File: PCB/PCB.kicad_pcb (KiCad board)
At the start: 2 copper layers, 120 x 60 mm, 62 parts, among them J1 USB_C_Receptacle_USB2.0_16P, J2 Conn_01x15, J3 Conn_01x15, Q2 IRLML2060, SW1 TSA016A2526B, SW2 TSA016A2526B, SW3 TSA016A2526B, U1 RP2040, U2 USBLC6-2SC6, U3 NCP1117ST33T3G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

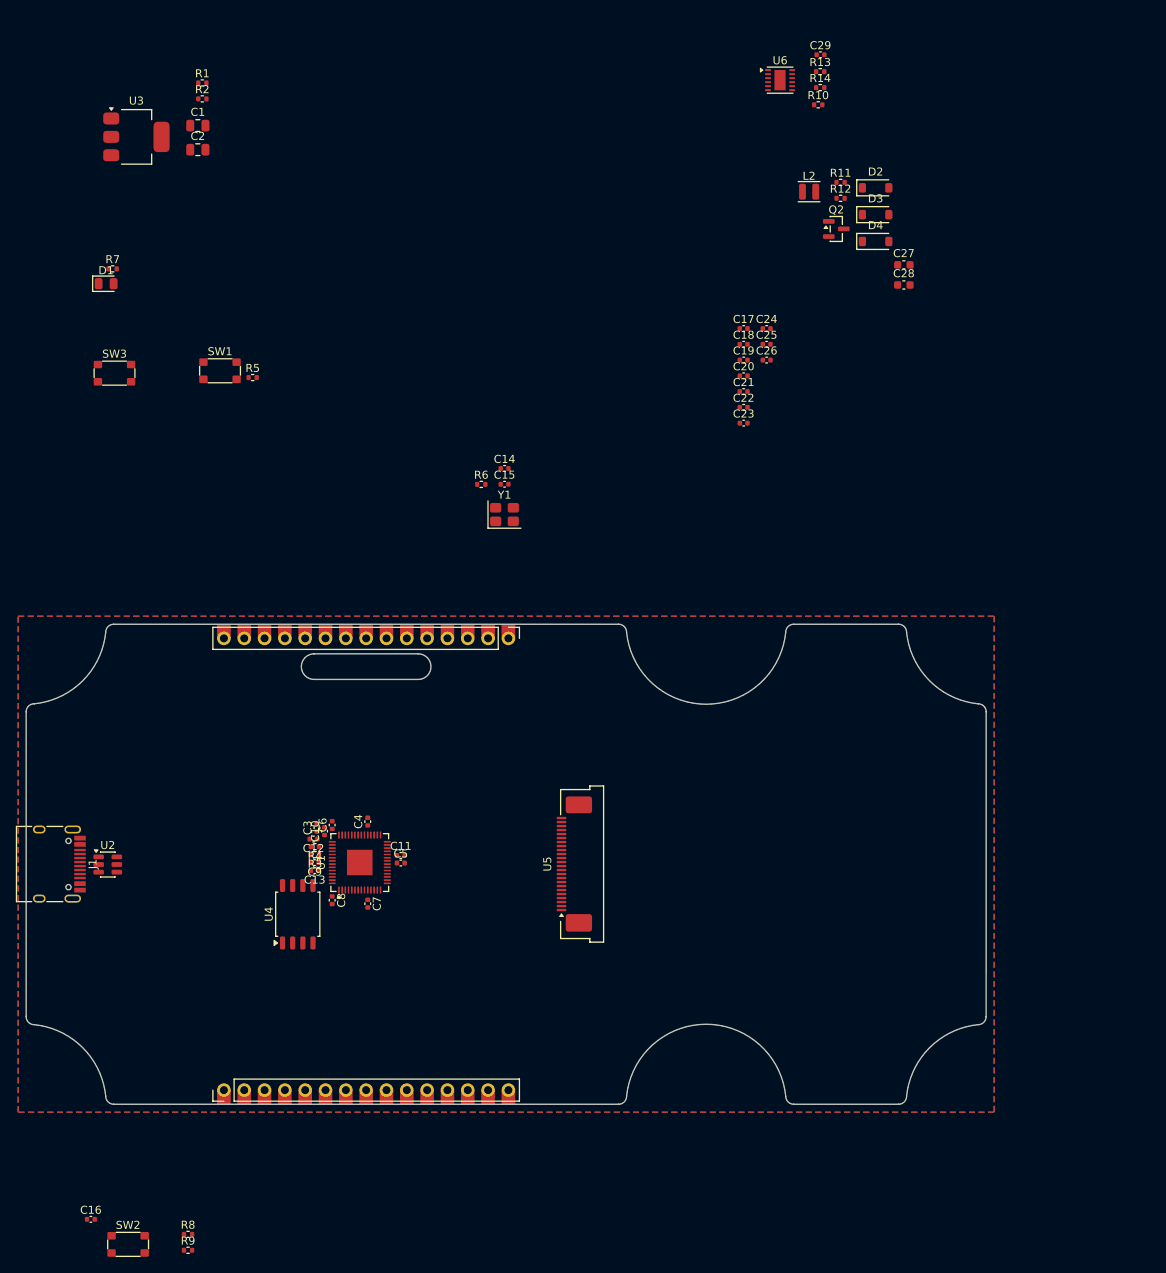
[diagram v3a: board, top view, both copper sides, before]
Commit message: aligning crystal and LDO
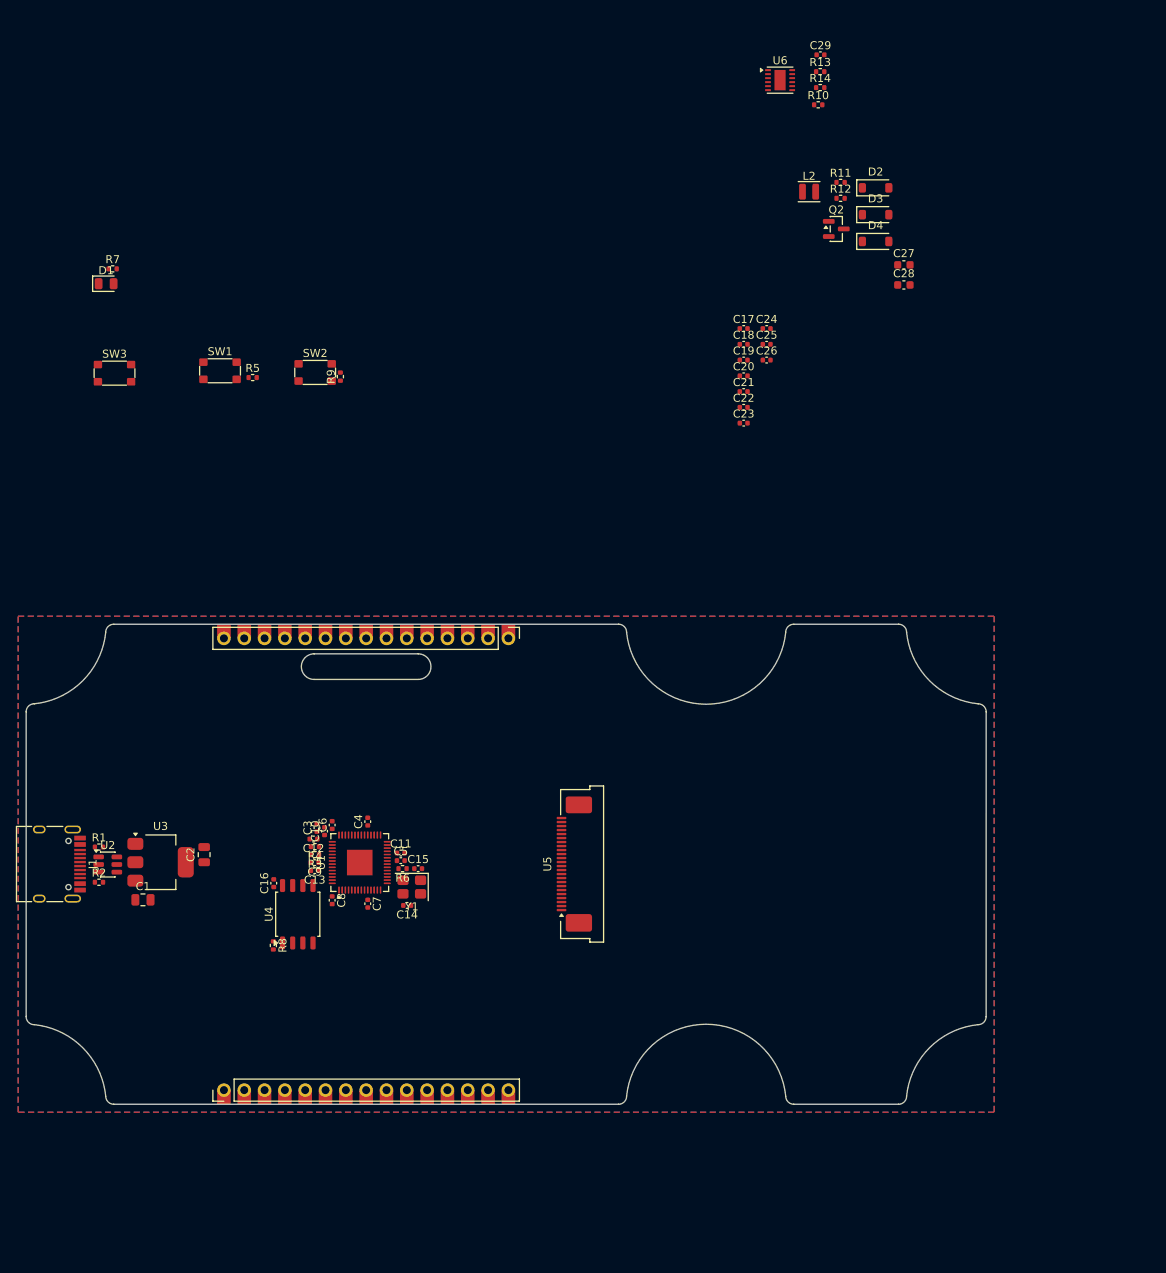
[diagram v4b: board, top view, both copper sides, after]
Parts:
- moved SW2 111.5 mm to (106.1, 63.5)
- moved R9 110.9 mm to (109.3, 64.0), turned to 90 degrees
- moved R2 98.8 mm to (79.1, 127.2)
- moved C1 97.0 mm to (84.6, 129.4)
- moved R1 96.4 mm to (79.1, 122.8)
- moved U3 90.7 mm to (86.8, 124.8)
- moved C2 88.1 mm to (92.2, 123.8), turned to 90 degrees
- moved C14 56.0 mm to (117.6, 130.2), turned to 180 degrees
- moved C15 49.2 mm to (119.0, 125.5)
- moved R6 49.0 mm to (117.0, 125.5), turned to 180 degrees
- moved Y1 48.0 mm to (118.2, 127.8), turned to 180 degrees
- moved C16 47.8 mm to (101.0, 127.4), turned to 90 degrees
- moved R8 37.7 mm to (100.9, 135.2), turned to -90 degrees
- moved C11 0.30 mm to (116.8, 123.6)
- moved C5 0.30 mm to (116.8, 124.5)

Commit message: aligning eink stuff
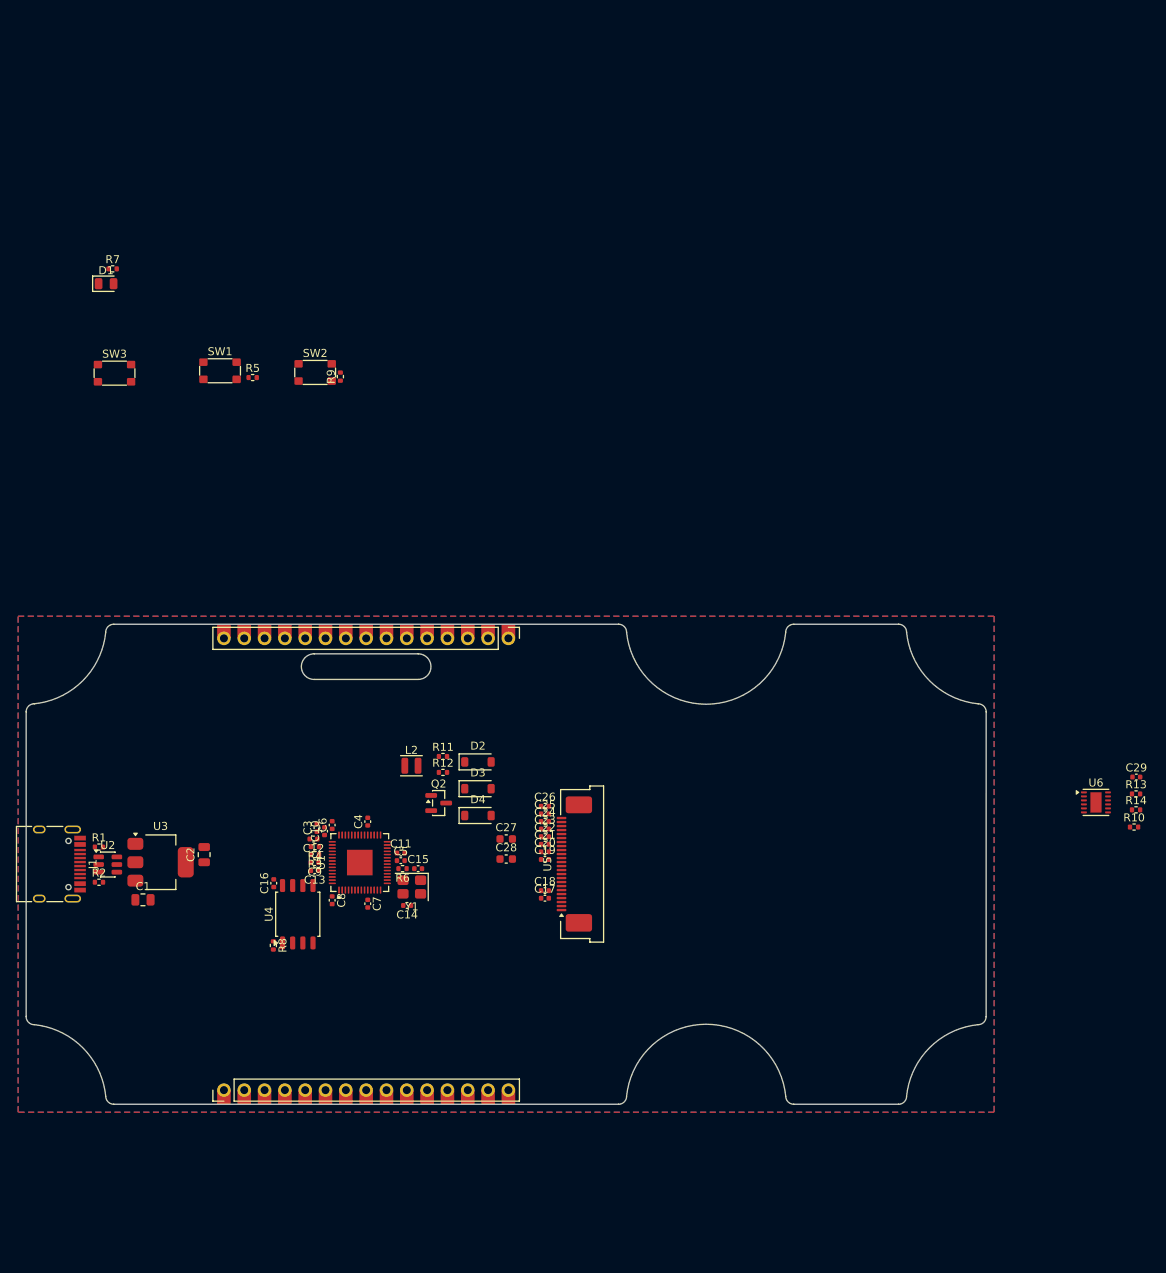
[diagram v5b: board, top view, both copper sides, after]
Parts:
- moved C29 98.5 mm to (208.8, 114.1)
- moved R10 98.5 mm to (208.5, 120.3)
- moved R13 98.5 mm to (208.7, 116.2)
- moved R14 98.5 mm to (208.7, 118.2)
- moved U6 98.5 mm to (203.7, 117.3)
- moved C27 87.3 mm to (130.0, 121.8)
- moved C28 87.3 mm to (130.0, 124.3)
- moved D2 87.3 mm to (126.5, 112.2)
- moved D3 87.3 mm to (126.5, 115.6)
- moved D4 87.3 mm to (126.5, 118.9)
- moved L2 87.3 mm to (118.2, 112.7)
- moved Q2 87.3 mm to (121.6, 117.3)
- moved R11 87.3 mm to (122.1, 111.5)
- moved R12 87.3 mm to (122.1, 113.5)
- moved C17 75.4 mm to (134.8, 129.2)
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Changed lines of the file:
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@@
 	(footprint "Capacitor_SMD:C_0402_1005Metric"
 		(layer "F.Cu")
-		(at 162.56 61.98)
+		(at 134.85 117.75)
 		(descr "Capacitor SMD 0402 (1005 Metric), square (rectangular) end terminal, IPC-7351 nominal, (Body size source: IPC-SM-782 page 76, https://www.pcb-3d.com/wordpress/wp-content/uploads/ipc-sm-782a_amendment_1_and_2.pdf), generated with kicad-footprint-generator")
 		(tags "capacitor")
@@
 	(footprint "Diode_SMD:D_SOD-123"
 		(layer "F.Cu")
-		(at 176.18 40.45)
+		(at 126.475 112.21)
 		(descr "SOD-123")
 		(tags "SOD-123")
@@
 	(footprint "Capacitor_SMD:C_0402_1005Metric"
 		(layer "F.Cu")
-		(at 169.2875 23.82)
+		(at 208.77 114.1)
 		(descr "Capacitor SMD 0402 (1005 Metric), square (rectangular) end terminal, IPC-7351 nominal, (Body size source: IPC-SM-782 page 76, https://www.pcb-3d.com/wordpress/wp-content/uploads/ipc-sm-782a_amendment_1_and_2.pdf), generated with kicad-footprint-generator")
 		(tags "capacitor")
@@
 	(footprint "Inductor_SMD:L_Sunlord_SWPA252010S"
 		(layer "F.Cu")
-		(at 167.865 40.93)
+		(at 118.16 112.69)
 		(descr "Inductor, Sunlord, SWPA252010S, 2.5x2.0x1.0mm, (https://www.sunlordinc.com/UploadFiles/PDF_Cat/20120704094224784.pdf), generated with kicad-footprint-generator gen_inductor.py")
 		(tags "swpa")
@@
 	(footprint "Resistor_SMD:R_0402_1005Metric"
 		(layer "F.Cu")
-		(at 169.255 27.92)
+		(at 208.7375 118.2)
 		(descr "Resistor SMD 0402 (1005 Metric), square (rectangular) end terminal, IPC-7351 nominal, (Body size source: IPC-SM-782 page 72, https://www.pcb-3d.com/wordpress/wp-content/uploads/ipc-sm-782a_amendment_1_and_2.pdf), generated with kicad-footprint-generator")
 		(tags "resistor")
@@
 	(footprint "Capacitor_SMD:C_0402_1005Metric"
 		(layer "F.Cu")
-		(at 162.56 58.04)
+		(at 134.85 119.65)
 		(descr "Capacitor SMD 0402 (1005 Metric), square (rectangular) end terminal, IPC-7351 nominal, (Body size source: IPC-SM-782 page 76, https://www.pcb-3d.com/wordpress/wp-content/uploads/ipc-sm-782a_amendment_1_and_2.pdf), generated with kicad-footprint-generator")
 		(tags "capacitor")
@@
 	(footprint "Diode_SMD:D_SOD-123"
 		(layer "F.Cu")
-		(at 176.18 47.15)
+		(at 126.475 118.91)
 		(descr "SOD-123")
 		(tags "SOD-123")
@@
 	(footprint "Capacitor_SMD:C_0402_1005Metric"
 		(layer "F.Cu")
-		(at 159.69 60.01)
+		(at 134.85 128.3)
 		(descr "Capacitor SMD 0402 (1005 Metric), square (rectangular) end terminal, IPC-7351 nominal, (Body size source: IPC-SM-782 page 76, https://www.pcb-3d.com/wordpress/wp-content/uploads/ipc-sm-782a_amendment_1_and_2.pdf), generated with kicad-footprint-generator")
 		(tags "capacitor")
@@
 	(footprint "Capacitor_SMD:C_0402_1005Metric"
 		(layer "F.Cu")
-		(at 159.69 58.04)
+		(at 134.85 129.25)
 		(descr "Capacitor SMD 0402 (1005 Metric), square (rectangular) end terminal, IPC-7351 nominal, (Body size source: IPC-SM-782 page 76, https://www.pcb-3d.com/wordpress/wp-content/uploads/ipc-sm-782a_amendment_1_and_2.pdf), generated with kicad-footprint-generator")
 		(tags "capacitor")
@@
 	(footprint "Package_TO_SOT_SMD:SOT-23"
 		(layer "F.Cu")
-		(at 171.2675 45.59)
+		(at 121.5625 117.35)
 		(descr "SOT, 3 Pin (JEDEC TO-236 Var AB https://www.jedec.org/document_search?search_api_views_fulltext=TO-236), generated with kicad-footprint-generator ipc_gullwing_generator.py")
 		(tags "SOT TO_SOT_SMD")
@@
 	(footprint "Capacitor_SMD:C_0402_1005Metric"
 		(layer "F.Cu")
-		(at 159.69 61.98)
+		(at 134.85 124.4)
 		(descr "Capacitor SMD 0402 (1005 Metric), square (rectangular) end terminal, IPC-7351 nominal, (Body size source: IPC-SM-782 page 76, https://www.pcb-3d.com/wordpress/wp-content/uploads/ipc-sm-782a_amendment_1_and_2.pdf), generated with kicad-footprint-generator")
 		(tags "capacitor")
@@
 	(footprint "Capacitor_SMD:C_0603_1608Metric"
 		(layer "F.Cu")
-		(at 179.715 50.08)
+		(at 130.01 121.84)
 		(descr "Capacitor SMD 0603 (1608 Metric), square (rectangular) end terminal, IPC-7351 nominal, (Body size source: IPC-SM-782 page 76, https://www.pcb-3d.com/wordpress/wp-content/uploads/ipc-sm-782a_amendment_1_and_2.pdf), generated with kicad-footprint-generator")
 		(tags "capacitor")
@@
 	(footprint "Capacitor_SMD:C_0402_1005Metric"
 		(layer "F.Cu")
-		(at 159.69 67.89)
+		(at 134.85 121.55)
 		(descr "Capacitor SMD 0402 (1005 Metric), square (rectangular) end terminal, IPC-7351 nominal, (Body size source: IPC-SM-782 page 76, https://www.pcb-3d.com/wordpress/wp-content/uploads/ipc-sm-782a_amendment_1_and_2.pdf), generated with kicad-footprint-generator")
 		(tags "capacitor")
@@
 	(footprint "Diode_SMD:D_SOD-123"
 		(layer "F.Cu")
-		(at 176.18 43.8)
+		(at 126.475 115.56)
 		(descr "SOD-123")
 		(tags "SOD-123")
@@
 	(footprint "Capacitor_SMD:C_0603_1608Metric"
 		(layer "F.Cu")
-		(at 179.715 52.59)
+		(at 130.01 124.35)
 		(descr "Capacitor SMD 0603 (1608 Metric), square (rectangular) end terminal, IPC-7351 nominal, (Body size source: IPC-SM-782 page 76, https://www.pcb-3d.com/wordpress/wp-content/uploads/ipc-sm-782a_amendment_1_and_2.pdf), generated with kicad-footprint-generator")
 		(tags "capacitor")
@@
 	(footprint "Capacitor_SMD:C_0402_1005Metric"
 		(layer "F.Cu")
-		(at 162.56 60.01)
+		(at 134.85 118.7)
 		(descr "Capacitor SMD 0402 (1005 Metric), square (rectangular) end terminal, IPC-7351 nominal, (Body size source: IPC-SM-782 page 76, https://www.pcb-3d.com/wordpress/wp-content/uploads/ipc-sm-782a_amendment_1_and_2.pdf), generated with kicad-footprint-generator")
 		(tags "capacitor")
@@
 	(footprint "Capacitor_SMD:C_0402_1005Metric"
 		(layer "F.Cu")
-		(at 159.69 69.86)
+		(at 134.85 120.6)
 		(descr "Capacitor SMD 0402 (1005 Metric), square (rectangular) end terminal, IPC-7351 nominal, (Body size source: IPC-SM-782 page 76, https://www.pcb-3d.com/wordpress/wp-content/uploads/ipc-sm-782a_amendment_1_and_2.pdf), generated with kicad-footprint-generator")
 		(tags "capacitor")
@@
 	(footprint "Resistor_SMD:R_0402_1005Metric"
 		(layer "F.Cu")
-		(at 169.255 25.93)
+		(at 208.7375 116.21)
 		(descr "Resistor SMD 0402 (1005 Metric), square (rectangular) end terminal, IPC-7351 nominal, (Body size source: IPC-SM-782 page 72, https://www.pcb-3d.com/wordpress/wp-content/uploads/ipc-sm-782a_amendment_1_and_2.pdf), generated with kicad-footprint-generator")
 		(tags "resistor")
@@
 	(footprint "Resistor_SMD:R_0402_1005Metric"
 		(layer "F.Cu")
-		(at 169.0075 30.07)
+		(at 208.49 120.35)
 		(descr "Resistor SMD 0402 (1005 Metric), square (rectangular) end terminal, IPC-7351 nominal, (Body size source: IPC-SM-782 page 72, https://www.pcb-3d.com/wordpress/wp-content/uploads/ipc-sm-782a_amendment_1_and_2.pdf), generated with kicad-footprint-generator")
 		(tags "resistor")
@@
 	(footprint "Capacitor_SMD:C_0402_1005Metric"
 		(layer "F.Cu")
-		(at 159.69 63.95)
+		(at 134.85 123.45)
 		(descr "Capacitor SMD 0402 (1005 Metric), square (rectangular) end terminal, IPC-7351 nominal, (Body size source: IPC-SM-782 page 76, https://www.pcb-3d.com/wordpress/wp-content/uploads/ipc-sm-782a_amendment_1_and_2.pdf), generated with kicad-footprint-generator")
 		(tags "capacitor")
@@
 	(footprint "Capacitor_SMD:C_0402_1005Metric"
 		(layer "F.Cu")
-		(at 159.69 65.92)
+		(at 134.85 122.5)
 		(descr "Capacitor SMD 0402 (1005 Metric), square (rectangular) end terminal, IPC-7351 nominal, (Body size source: IPC-SM-782 page 76, https://www.pcb-3d.com/wordpress/wp-content/uploads/ipc-sm-782a_amendment_1_and_2.pdf), generated with kicad-footprint-generator")
 		(tags "capacitor")
@@
 	(footprint "Resistor_SMD:R_0402_1005Metric"
 		(layer "F.Cu")
-		(at 171.805 39.77)
+		(at 122.1 111.53)
 		(descr "Resistor SMD 0402 (1005 Metric), square (rectangular) end terminal, IPC-7351 nominal, (Body size source: IPC-SM-782 page 72, https://www.pcb-3d.com/wordpress/wp-content/uploads/ipc-sm-782a_amendment_1_and_2.pdf), generated with kicad-footprint-generator")
 		(tags "resistor")
@@
 	(footprint "Package_DFN_QFN:ST_UFDFPN-12-1EP_3x3mm_P0.5mm_EP1.4x2.55mm"
 		(layer "F.Cu")
-		(at 164.2425 26.99)
+		(at 203.725 117.27)
 		(descr "ST  UFDFPN, 12 Pin (https://www.st.com/resource/en/datasheet/st25dv04k.pdf#page=152), generated with kicad-footprint-generator ipc_noLead_generator.py")
 		(tags "ST UFDFPN NoLead")
@@
 	(footprint "Resistor_SMD:R_0402_1005Metric"
 		(layer "F.Cu")
-		(at 171.805 41.76)
+		(at 122.1 113.52)
 		(descr "Resistor SMD 0402 (1005 Metric), square (rectangular) end terminal, IPC-7351 nominal, (Body size source: IPC-SM-782 page 72, https://www.pcb-3d.com/wordpress/wp-content/uploads/ipc-sm-782a_amendment_1_and_2.pdf), generated with kicad-footprint-generator")
 		(tags "resistor")

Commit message: finished aligning the eink and LED
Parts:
- moved R7 72.2 mm to (81.3, 122.8), turned to 180 degrees
- moved D1 68.9 mm to (79.8, 121.3)
- moved L2 14.3 mm to (127.2, 123.7), turned to 90 degrees
- moved D2 9.35 mm to (129.8, 121.0), turned to 180 degrees
- moved R11 9.07 mm to (122.1, 120.6), turned to 180 degrees
- moved R12 8.98 mm to (122.1, 122.5), turned to 180 degrees
- moved Q2 5.44 mm to (125.0, 121.5)
- moved C27 4.94 mm to (126.7, 118.2), turned to -90 degrees
- moved D3 4.51 mm to (129.8, 118.6)
- moved D4 4.29 mm to (129.8, 116.2), turned to 180 degrees
- moved C28 0.95 mm to (129.3, 123.7), turned to -90 degrees
